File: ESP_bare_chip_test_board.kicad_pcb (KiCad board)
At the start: 4 copper layers, 57.1 x 69.8 mm, 167 parts, among them J1301 Conn_01x06, J1302 Conn_01x06, J1501 Conn_01x04, J1502 Conn_01x04, J201 Conn_01x06, J501 DAISY_CHAIN, J501 USB_C_Receptacle, J502 PWR_IN, J601 Conn_01x06, J801 USB_C_Receptacle, J802 USB_C_Receptacle, Q301 40MHz, Q501 DTC114E, Q502 DTC114E, Q701 40MHz, SW201 SW_Push, SW202 SW_Push, SW601 SW_Push, SW602 SW_Push, U1001 TLV62569DBV, U1101 TPS563201, U1401 W25Q128JVS, U1501 D1213A-04TS-7, U201 TLV75533PDBV, U202 ESP32-S3-MINI-1, U301 W25Q128JVS, U302 ESP32-S3, U401 MASWSS0179, U501 DT1240A-04LP-7, U501 TPS2552DBV, U502 FUSB302BMPX, U502 TPS2552DBV, U701 W25Q128JVS, U702 ESP32-C3, U702 ESP32-S3, U801 D1213A-04TS-7, U802 D1213A-04TS-7, U803 FUSB302BPX, U901 TLV62569DBV

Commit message: Uknown changes?File formats?
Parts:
- removed C204: 100nF/50V, Capacitor_SMD:C_0603_1608Metric
- removed C205: 22uF/6.3V, Capacitor_SMD:C_0603_1608Metric
- removed C505: 1uF/50V, Capacitor_SMD:C_0805_2012Metric
- removed the C703 at (79.4, 45.4)
- removed C708: 0.1uF, Capacitor_SMD:C_0402_1005Metric
- removed D202: GREEN, LED_SMD:LED_0603_1608Metric
- removed the J501 at (49.3, 5.30)
- removed the J501 at (97.9, 90.4)
- removed R508: 100kΩ, Resistor_SMD:R_0603_1608Metric
- removed R509: 33kΩ, Resistor_SMD:R_0603_1608Metric
- removed REF**: U.FL_Molex_MCRF_73412-0110_Vertical, Connector_Coaxial:U.FL_Molex_MCRF_73412-0110_Vertical
- removed U201: TLV75533PDBV, Package_TO_SOT_SMD:SOT-23-5
- removed U202: ESP32-S3-MINI-1, Espressif:ESP32-S3-MINI-1
- removed the U501 at (47.6, 18.5)
- removed the U501 at (103.1, 96.2)
- removed the U502 at (47.6, 23.0)
- removed the U502 at (94.8, 96.5)
- removed the U702 at (84.5, 48.1)
- added C701: 10pF, Capacitor_SMD:C_0603_1608Metric, F.Cu at (72.9, 69.9)
- added C702: 10pF, Capacitor_SMD:C_0603_1608Metric, F.Cu at (72.9, 72.4)
- added J1201: NorComp - 112-024-113RYY1, Connector_Centronics_custom:CENTRONICS-24, F.Cu at (58.4, 9.48)
- added J501: Barrel_Jack, Connector_BarrelJack:BarrelJack_CUI_PJ-063AH_Horizontal, F.Cu at (37.1, 39.3)
- added R101: 0, Resistor_SMD:R_0402_1005Metric, F.Cu at (53.3, 61.7)
- added R506: 33kΩ, Resistor_SMD:R_0603_1608Metric, F.Cu at (46.2, 41.6)
- added R507: 15kΩ, Resistor_SMD:R_0603_1608Metric, F.Cu at (46.2, 44.1)
- added U501: TPS2552DBV, Package_TO_SOT_SMD:SOT-23-6, F.Cu at (50.8, 43.2)
- added U502: TPS2552DBV, Package_TO_SOT_SMD:SOT-23-6, F.Cu at (50.8, 47.6)
- added U701: ESP32-C3, Package_DFN_QFN:QFN-32-1EP_5x5mm_P0.5mm_EP3.45x3.45mm, F.Cu at (69.3, 65.0)
- C202: value 1uF/50V -> 100nF/50V; footprint Capacitor_SMD:C_0805_2012Metric -> Capacitor_SMD:C_0603_1608Metric
- C203: value 4.7uF/25V -> 22uF/6.3V; footprint Capacitor_SMD:C_0805_2012Metric -> Capacitor_SMD:C_0603_1608Metric
- C705: value 10nF -> 1uF
- C707: value 0.1uF -> 10nF
- C709, C710: value 10pF -> 0.1uF; footprint Capacitor_SMD:C_0603_1608Metric -> Capacitor_SMD:C_0402_1005Metric
- D201: value B5819W -> GREEN; footprint Diode_SMD:D_SOD-123 -> LED_SMD:LED_0603_1608Metric
- D502: value YELLOW -> SS210; footprint LED_SMD:LED_0603_1608Metric -> Diode_SMD:D_SMA
- D503, D504: value GREEN -> SS210; footprint LED_SMD:LED_0603_1608Metric -> Diode_SMD:D_SMA
- D506, D507: value SS210 -> GREEN; footprint Diode_SMD:D_SMA -> LED_SMD:LED_0603_1608Metric
- D508: value SS210 -> YELLOW; footprint Diode_SMD:D_SMA -> LED_SMD:LED_0603_1608Metric
- R503: value 10kΩ -> 100kΩ
- R504: value 15kΩ/1% -> 10kΩ
- R505: value 15kΩ -> 15kΩ/1%
- moved U401 87.6 mm to (54.4, 56.5), turned to 0 degrees
- moved C805 68.4 mm to (43.6, 63.1)
- moved U802 68.4 mm to (44.1, 71.5)
- moved C801 68.4 mm to (43.6, 55.3)
- moved C802 68.4 mm to (43.6, 57.2)
- moved C803 68.4 mm to (43.6, 59.2)
- moved C804 68.4 mm to (43.6, 61.2)
- moved J801 68.4 mm to (36.4, 59.3)
- moved J802 68.4 mm to (36.0, 68.5)
- moved U801 68.4 mm to (44.1, 67.0)
- moved U803 68.4 mm to (47.4, 56.7)
- moved D201 60.6 mm to (90.6, 32.4)
- moved SW201 58.9 mm to (91.8, 24.8)
- moved SW202 58.9 mm to (91.8, 29.0)
- moved C203 56.5 mm to (86.5, 29.0)
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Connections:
- C202 pad 1: Net-(D201-K) -> +3V3
- C709 pad 1: Net-(U702-XTAL_N) -> 3v3_{AUX}
- C709 pad 2: Net-(C709-Pad2) -> GND
- C710 pad 1: Net-(C710-Pad1) -> 3v3_{AUX}
- C710 pad 2: Net-(C710-Pad2) -> GND
- D201 pad 2: +5V -> +3V3
- D502 pad 1: Net-(D502-K) -> /Power/step-down-12v-5v/V_{IN}
- D502 pad 2: 3v3_{LED} -> /Power/12V_IN
- D503 pad 1: Net-(D503-K) -> /Power/step-down-12v-5v/V_{IN}
- D503 pad 2: +12V -> Net-(D503-A)
- D504 pad 1: Net-(D504-K) -> /Power/12V_IN
- D504 pad 2: +5V -> GND
- D505 pad 1: /Power/step-down-12v-5v/V_{IN} -> Net-(D503-A)
- D505 pad 2: /Power/12V_IN -> GND
- D506 pad 1: /Power/step-down-12v-5v/V_{IN} -> Net-(D506-K)
- D506 pad 2: Net-(D506-A) -> +12V
- D507 pad 1: /Power/12V_IN -> Net-(D507-K)
- D507 pad 2: GND -> +5V
- D508 pad 1: Net-(D506-A) -> Net-(D508-K)
- D508 pad 2: GND -> 3v3_{LED}
- J502 pad 2: Net-(D506-A) -> Net-(D503-A)
- J801 pad A6: /USB/D+ -> /USB_D+
- J801 pad A7: /USB/D- -> /USB_D-
- J801 pad B6: /USB/D+ -> /USB_D+
- J801 pad B7: /USB/D- -> /USB_D-
- J802 pad A6: /USB/D+ -> /USB_D+
- J802 pad A7: /USB/D- -> /USB_D-
- J802 pad B6: /USB/D+ -> /USB_D+
- J802 pad B7: /USB/D- -> /USB_D-
- Q701 pad 1: Net-(U702-XTAL_N) -> Net-(U701-XTAL_N)
- Q701 pad 2: Net-(C710-Pad2) -> Net-(C702-Pad2)
- Q701 pad 3: Net-(C710-Pad1) -> Net-(C702-Pad1)
- Q701 pad 4: Net-(C709-Pad2) -> Net-(C701-Pad2)
- R202 pad 1: Net-(D202-K) -> Net-(D201-K)
- R503 pad 1: /Power/~{SINK_EN} -> Net-(D506-K)
- R503 pad 2: GND -> Net-(Q501-C)
- R504 pad 1: Net-(U502-ILIM) -> /Power/~{SINK_EN}
- R505 pad 1: Net-(D502-K) -> Net-(U502-ILIM)
- R505 pad 2: /Power/~{SOURCE_EN} -> GND
- R603 pad 2: /ESP32-C3/IO8/STRAP^{PU} -> /esp2esp_CS
- R701 pad 1: Net-(C710-Pad1) -> Net-(C702-Pad1)
- U302 pad 38: /ESP32-S3/IO33 -> I2C0.SDA
- U302 pad 39: /ESP32-S3/IO34 -> I2C0.SCL
- U302 pad 51: /ESP32-S3/IO45 -> I2C0.INT
- U801 pad 1: /USB/D+ -> /USB_D+
- U801 pad 6: /USB/D- -> /USB_D-
- U802 pad 1: /USB/D+ -> /USB_D+
- U802 pad 6: /USB/D- -> /USB_D-
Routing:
- net /ESP32-S3/IO45: track 7.47 -> 0.00 mm, vias 2 -> 0
- net (no net): track 117.8 -> 121.6 mm, vias 32 -> 33
- net I2C0.INT: track 0.00 -> 3.73 mm, vias 0 -> 1

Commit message: Unknown changes? Arranging components, I believe
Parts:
- removed C601, C602: 100nF/50V, Capacitor_SMD:C_0603_1608Metric
- removed C603, C903: 22uF/6.3V, Capacitor_SMD:C_0603_1608Metric
- removed the C701 at (72.9, 69.9)
- removed the C702 at (72.9, 72.4)
- removed C705: 1uF, Capacitor_SMD:C_0402_1005Metric
- removed the C707 at (64.2, 64.3)
- removed the C709 at (64.2, 66.3)
- removed the C710 at (64.2, 68.2)
- removed C901: 10uF/10V, Capacitor_SMD:C_0603_1608Metric
- removed C902: 22pF, Capacitor_SMD:C_0402_1005Metric
- removed J601: Conn_01x06, Connector_PinSocket_2.54mm:PinSocket_1x06_P2.54mm_Vertical
- removed L901: 2.2uH, Inductor_SMD:L_Changjiang_FNR252012S
- removed the Q701 at (68.3, 70.9)
- removed R101: 0, Resistor_SMD:R_0402_1005Metric
- removed R601: 10kΩ, Resistor_SMD:R_0603_1608Metric
- removed R602, R603: 100kΩ, Resistor_SMD:R_0603_1608Metric
- removed R701: TBD, 24nH to start, Resistor_SMD:R_0402_1005Metric
- removed R901: 150kΩ, Resistor_SMD:R_0603_1608Metric
- removed R902: 33kΩ, Resistor_SMD:R_0603_1608Metric
- removed SW601, SW602: SW_Push, Button_Switch_SMD_custom:SW_PUSHBUTTON_2PIN_SMD_3×4×2.0
- removed the U701 at (69.3, 65.0)
- removed U901: TLV62569DBV, Package_TO_SOT_SMD:SOT-23-5
- added J503: ALTERNATE, Connector_TerminalBlock_custom:Ningbo_Xinlaiya_XY2500R-D-5.08-2P_1x02_P5.08mm_Horizontal, F.Cu at (123.2, 83.8)
- added REF**: USR-ES1, Module_custom:USR-ES1, F.Cu at (111.8, 97.8)
- moved J1201 125.2 mm to (160.4, 82.1), turned to 90 degrees
- moved J502 121.6 mm to (130.8, 101.0)
- moved J501 109.5 mm to (125.2, 104.1), turned to -90 degrees
- moved D502 97.4 mm to (129.5, 84.5), turned to 180 degrees
- moved D503 97.0 mm to (129.5, 88.3), turned to 180 degrees
- moved D505 93.9 mm to (129.5, 92.1)
- moved J1501 93.1 mm to (152.4, 107.3)
- moved D504 90.2 mm to (129.5, 80.6)
- moved J201 87.1 mm to (153.7, 74.9), turned to 180 degrees
- moved J801 84.2 mm to (120.0, 68.6), turned to -90 degrees
- moved U802 83.0 mm to (127.0, 68.6), turned to 90 degrees
- moved U803 80.2 mm to (127.3, 63.9)
- moved J802 78.4 mm to (-5.86, 2.29)
- moved U801 77.2 mm to (-5.91, 8.24)
- moved D507 64.5 mm to (6.00, 3.38)
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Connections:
- net /ESP32-C3/UART0_Rx renamed /ESP32-S3/UART0_Tx
- net /ESP32-C3/UART0_Tx renamed /ESP32-S3/UART0_Rx
- net /Power/12V_IN renamed /Power/V_{IN}_Left
- net /Power/step-down-12v-5v/V_{IN} renamed /Power/V_{IN}
- D503 pad 2: Net-(D503-A) -> /Power/V_{IN}_Right
- D505 pad 1: Net-(D503-A) -> /Power/V_{IN}_Right
- J1201 pad 1: /connector_GPIB/B1 -> /ESP32-S3/IO42
- J1201 pad 10: /connector_GPIB/SRQ -> /ESP32-S3/IO3
- J1201 pad 11: /connector_GPIB/ATN -> /ESP32-S3/IO2
- J1201 pad 13: /connector_GPIB/B5 -> /ESP32-S3/IO17
- J1201 pad 14: /connector_GPIB/B6 -> /ESP32-S3/IO16
- J1201 pad 15: /connector_GPIB/B7 -> /ESP32-S3/IO15
- J1201 pad 16: /connector_GPIB/B8 -> /ESP32-S3/IO14
- J1201 pad 17: /connector_GPIB/REN -> /ESP32-S3/IO1
- J1201 pad 2: /connector_GPIB/B2 -> /ESP32-S3/IO41
- J1201 pad 3: /connector_GPIB/B3 -> /ESP32-S3/IO21
- J1201 pad 4: /connector_GPIB/B4 -> /ESP32-S3/IO18
- J1201 pad 5: /connector_GPIB/EOI -> /ESP32-S3/IO8
- J1201 pad 6: /connector_GPIB/DAV -> /ESP32-S3/IO7
- J1201 pad 7: /connector_GPIB/NRFD -> /ESP32-S3/IO6
- J1201 pad 8: /connector_GPIB/NDAC -> /ESP32-S3/IO5
- J1201 pad 9: /connector_GPIB/IFC -> /ESP32-S3/IO4
- J1501 pad 3: /piicodev_connectors/J0_pin3 -> /ESP32-S3/IO37
- J1501 pad 4: /piicodev_connectors/J0_pin4 -> /ESP32-S3/IO38
- J1502 pad 3: /piicodev_connectors/J1_pin3 -> /ESP32-S3/IO35
- J1502 pad 4: /piicodev_connectors/J1_pin4 -> /ESP32-S3/IO36
- J501 pad 2: Net-(D503-A) -> /Power/V_{IN}_Right
- J501 pad MP: Net-(D503-A) -> GND
- J502 pad 2: Net-(D503-A) -> /Power/V_{IN}_Right
- U1501 pad 1: /piicodev_connectors/J0_pin3 -> /ESP32-S3/IO37
- U1501 pad 3: /piicodev_connectors/J0_pin4 -> /ESP32-S3/IO38
- U1501 pad 4: /piicodev_connectors/J1_pin3 -> /ESP32-S3/IO35
- U1501 pad 6: /piicodev_connectors/J1_pin4 -> /ESP32-S3/IO36
- U302 pad 36: /ESP32-S3/IO48 -> /ESP32-S3/IO37
- U302 pad 37: /ESP32-S3/IO47 -> /ESP32-S3/IO38
- U302 pad 44: /ESP32-S3/IO39 -> /ESP32-S3/IO35
- U302 pad 45: /ESP32-S3/IO40 -> /ESP32-S3/IO36
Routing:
- net (no net): track 121.6 -> 145.2 mm, vias 33 -> 24
- net /ESP32-S3/IO39: track 15.0 -> 0.00 mm
- net /ESP32-S3/IO40: track 14.9 -> 0.00 mm
- net /ESP32-S3/ESP32-S3-core/VDD_SPI: track 15.8 -> 28.9 mm, vias 1 -> 2
- net /Power/V_{IN}_Right: track 0.00 -> 8.69 mm
- net /Power/V_{IN}_Left: track 0.00 -> 8.69 mm
- net GND: track 1.72 -> 9.60 mm, vias 2 -> 35
- net +3V3: track 4.02 -> 10.1 mm, vias 0 -> 1
- net /Power/V_{IN}: track 0.00 -> 5.62 mm, vias 0 -> 1
- net /USB_D+: track 17.7 -> 22.1 mm, vias 0 -> 2
- net /ESP32-S3/IO38: track 0.00 -> 4.39 mm, vias 0 -> 1
- net /ESP32-S3/IO42: track 21.6 -> 24.7 mm, vias 0 -> 1
- net /ESP32-S3/IO36: track 0.00 -> 3.02 mm, vias 0 -> 1
- net /USB_D-: track 21.5 -> 24.2 mm
- net /ESP32-S3/IO35: track 0.00 -> 2.50 mm, vias 0 -> 1
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- added copper zone on B.Cu, net GND
- added copper zone on F.Cu, net GND
- added copper zone on In1.Cu, net GND
- added copper zone on In2.Cu, net GND
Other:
- board size 57.1 x 69.8 mm -> 57.1 x 63.5 mm

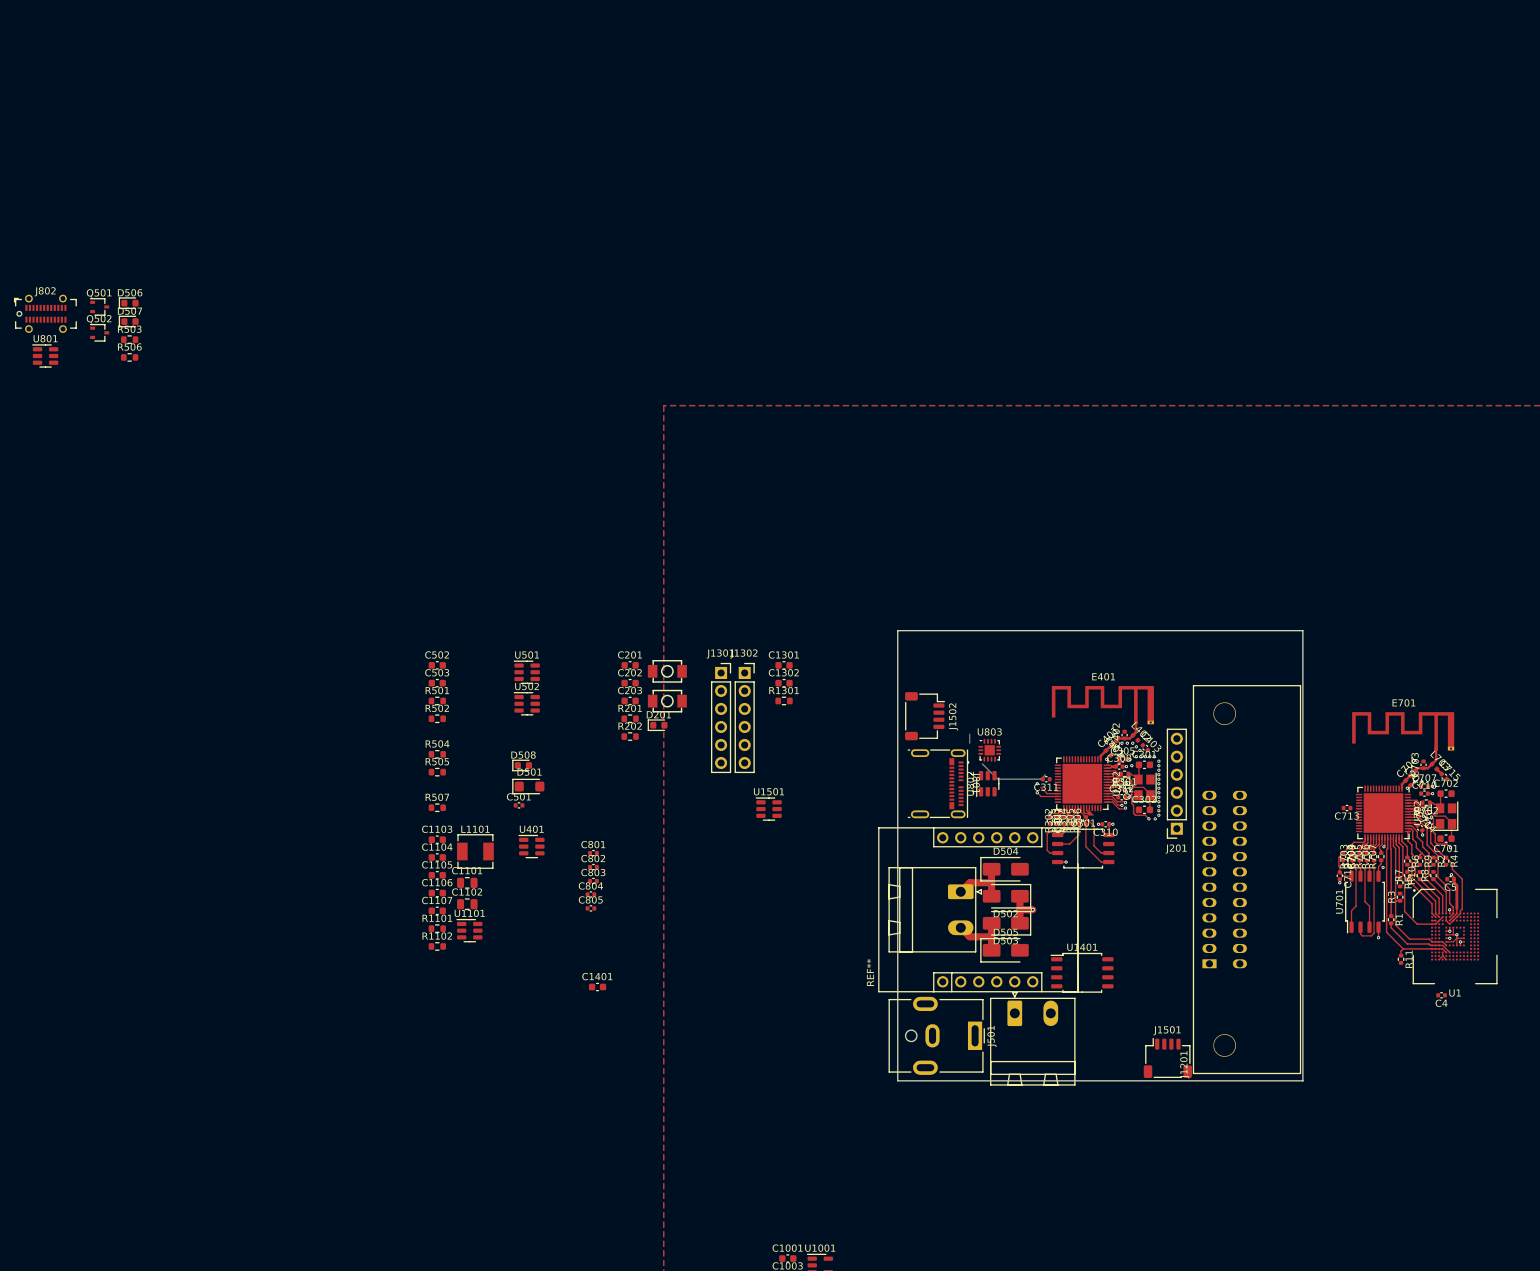
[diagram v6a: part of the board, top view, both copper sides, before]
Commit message: Arranged buck-boost regulator. Moved some components slightly.
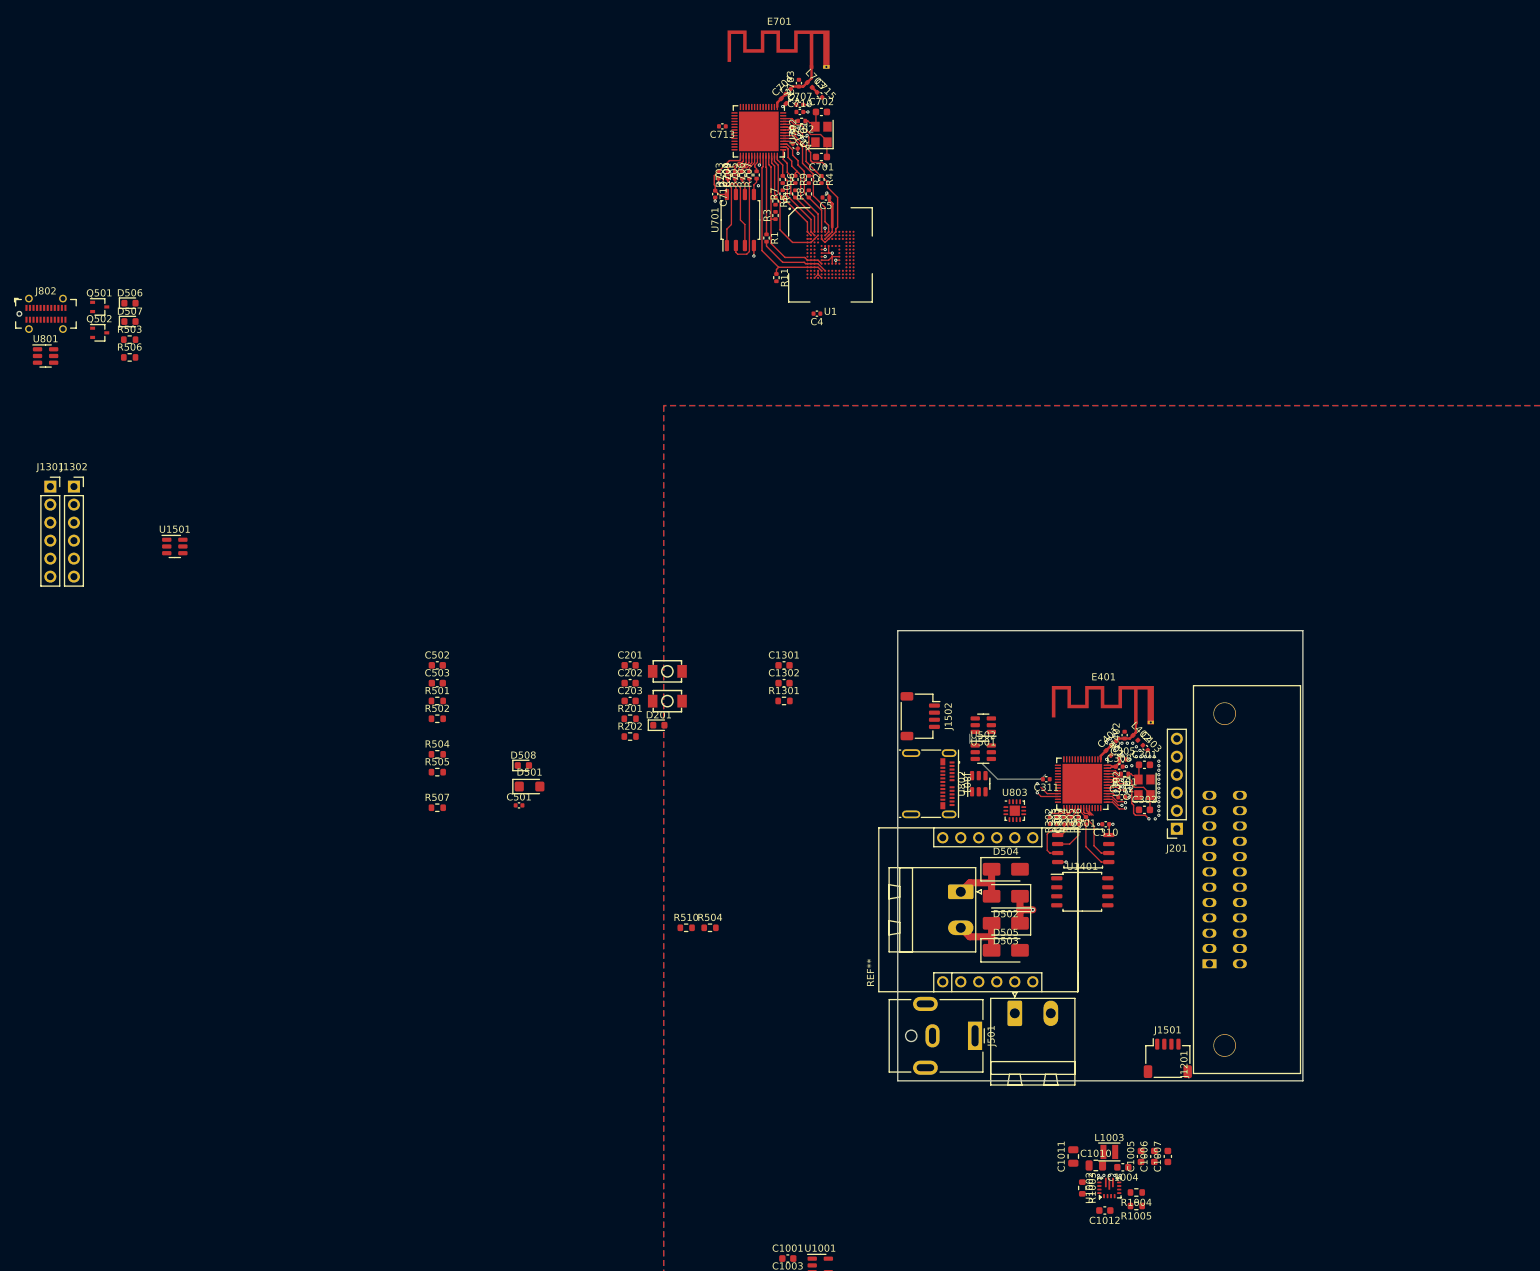
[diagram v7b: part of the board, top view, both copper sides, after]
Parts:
- removed C1101, C1102: 10uF/25v, Capacitor_SMD:C_0805_2012Metric
- removed C1103: 100nF, Capacitor_SMD:C_0603_1608Metric
- removed C1104, C1105, C1106, C1107: 10uF/10V, Capacitor_SMD:C_0603_1608Metric
- removed C1401: 100nF/50V, Capacitor_SMD:C_0603_1608Metric
- removed C801, C803: 220pF, Capacitor_SMD:C_0402_1005Metric
- removed C802, C804: 100nF/50V, Capacitor_SMD:C_0402_1005Metric
- removed C805: 1uF/25V, Capacitor_SMD:C_0402_1005Metric
- removed L1101: 3.3uH/1.2mΩ, Inductor_SMD:L_Sunlord_MWSA0402S
- removed R1101: 56kΩ/1%, Resistor_SMD:R_0603_1608Metric
- removed R1102: 10kΩ/1%, Resistor_SMD:R_0603_1608Metric
- removed U1101: TPS563201, Package_TO_SOT_SMD:SOT-23-6
- removed U401: MASWSS0179, Package_TO_SOT_SMD:SOT-23-6
- added C1004: 10uF/10V, Capacitor_SMD:C_0603_1608Metric, F.Cu at (146.1, 122.7)
- added C1005: 10uF/10V, Capacitor_SMD:C_0603_1608Metric, F.Cu at (148.6, 121.2)
- added C1006: 10uF/10V, Capacitor_SMD:C_0603_1608Metric, F.Cu at (150.5, 121.2)
- added C1007: 10uF/10V, Capacitor_SMD:C_0603_1608Metric, F.Cu at (152.4, 121.2)
- added C1010: 10uF/25v, Capacitor_SMD:C_0805_2012Metric, F.Cu at (142.2, 122.4)
- added C1011: 10uF/25v, Capacitor_SMD:C_0805_2012Metric, F.Cu at (139.1, 121.2)
- added C1012: 100nF, Capacitor_SMD:C_0603_1608Metric, F.Cu at (143.5, 128.8)
- added L1003: 1.5uH, Inductor_SMD:L_Changjiang_FNR252012S, F.Cu at (144.1, 120.5)
- added R1003: 100kΩ, Resistor_SMD:R_0603_1608Metric, F.Cu at (140.3, 125.6)
- added R1004: 680kΩ, Resistor_SMD:R_0603_1608Metric, F.Cu at (148.0, 126.2)
- added R1005: 130kΩ, Resistor_SMD:R_0603_1608Metric, F.Cu at (148.0, 128.1)
- added R504: 33kΩ, Resistor_SMD:R_0603_1608Metric, F.Cu at (87.8, 88.9)
- added R510: 100kΩ, Resistor_SMD:R_0603_1608Metric, F.Cu at (84.5, 88.9)
- added U1002: TPS63070, Package_DFN_QFN_custom:VQFN-15-HR_2.5x3mm_P0.5mm, F.Cu at (144.1, 125.6)
- moved C701 130.4 mm to (103.5, -19.8)
- moved C702 130.4 mm to (103.5, -26.2)
- moved C707 130.4 mm to (100.5, -27.2)
- moved C710 130.4 mm to (100.5, -26.2)
- moved C713 130.4 mm to (89.6, -24.1)
- moved C714 130.4 mm to (99.9, -21.4)
- moved E701 130.4 mm to (102.1, -32.5)
- moved L701 130.4 mm to (98.2, -27.7)
- moved Q701 130.4 mm to (103.5, -23.0)
- moved R10 130.4 mm to (99.9, -14.6)
- moved R11 130.4 mm to (97.2, -2.81)
- moved R2 130.4 mm to (101.8, -16.7)
- moved R4 130.4 mm to (103.5, -16.7)
- moved R703 130.4 mm to (90.3, -17.3)
- moved R706 130.4 mm to (93.4, -17.3)
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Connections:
- net /USB/USB_VBUS renamed /Power/VBUS
- U502 pad 3: /Power/~{SINK_EN} -> /Power/buck-boost-5v/PGOOD
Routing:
- net (no net): vias 24 -> 31
